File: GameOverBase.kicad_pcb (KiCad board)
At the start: 4 copper layers, 50 x 35 mm, 49 parts, among them J1 USB_C_DEALON-USB-US31-106, J2 Serial Port, J3 add-on conn, Q1 PMN48XP, SW1 SW_DIP_x08, SW2 boot, SW3 Reset, U1 ESP32-WROOM-E, U2 4021, U3 MCP73831-2ACI-OT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

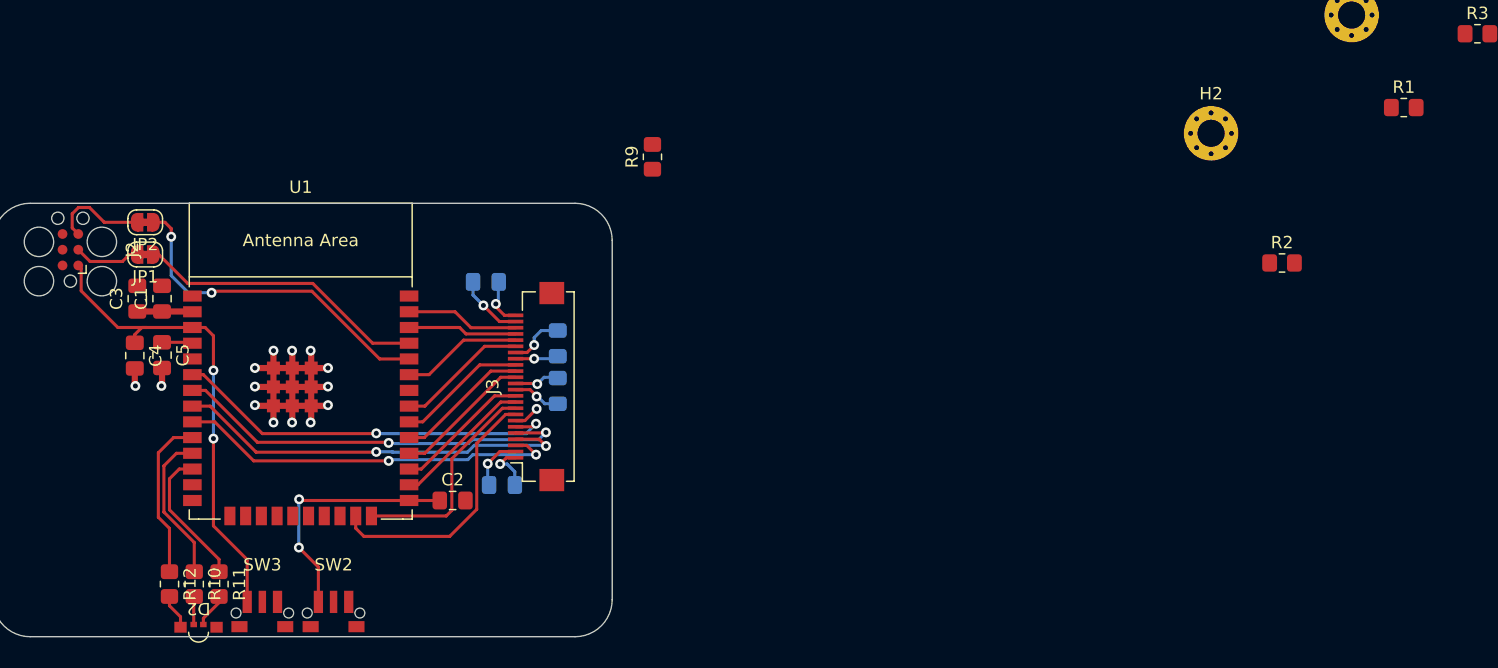
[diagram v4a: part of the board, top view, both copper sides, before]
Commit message: Brings in resistors for the ESP_BOOT and ESP_EN lines that were missing
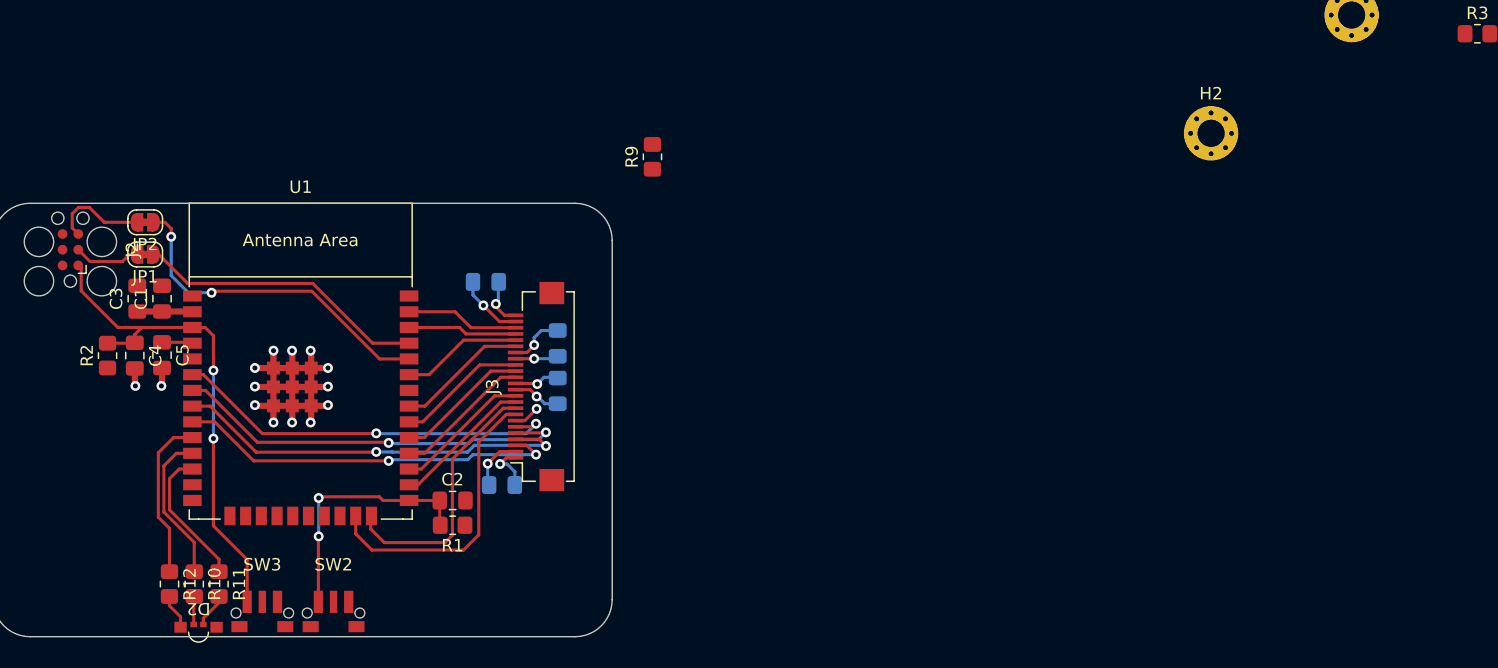
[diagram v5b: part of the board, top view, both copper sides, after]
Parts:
- moved R2 95.1 mm to (129.2, 92.3), turned to 90 degrees
- moved R1 83.9 mm to (157.1, 106.0), turned to 180 degrees
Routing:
- net IO2: track 17.7 -> 21.3 mm
- net IO15: track 21.4 -> 23.8 mm
- net ESP_EN: track 38.8 -> 41.0 mm
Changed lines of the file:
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@@
   )
   (footprint "Resistor_SMD:R_0805_2012Metric_Pad1.20x1.40mm_HandSolder" (layer "F.Cu")
-    (at 233.92 72.27)
+    (at 157.1125 106 180)
     (descr "Resistor SMD 0805 (2012 Metric), square (rectangular) end terminal, IPC_7351 nominal with elongated pad for handsoldering. (Body size source: IPC-SM-782 page 72, https://www.pcb-3d.com/wordpress/wp-content/uploads/ipc-sm-782a_amendment_1_and_2.pdf), generated with kicad-footprint-generator")
     (tags "resistor handsolder")
@@
     (fp_line (start 1 0.625) (end -1 0.625)
       (stroke (width 0.1) (type solid)) (layer "F.Fab"))
-    (pad "1" smd roundrect (at -1 0) (size 1.2 1.4) (layers "F.Cu" "F.Paste" "F.Mask") (roundrect_rratio 0.208333)
+    (pad "1" smd roundrect (at -1 0 180) (size 1.2 1.4) (layers "F.Cu" "F.Paste" "F.Mask") (roundrect_rratio 0.208333)
       (net 3 "+3V3") (pintype "passive"))
-    (pad "2" smd roundrect (at 1 0) (size 1.2 1.4) (layers "F.Cu" "F.Paste" "F.Mask") (roundrect_rratio 0.208333)
+    (pad "2" smd roundrect (at 1 0 180) (size 1.2 1.4) (layers "F.Cu" "F.Paste" "F.Mask") (roundrect_rratio 0.208333)
       (net 4 "ESP_BOOT") (pintype "passive"))
     (model "${KICAD6_3DMODEL_DIR}/Resistor_SMD.3dshapes/R_0805_2012Metric.wrl"
@@
   )
   (footprint "Resistor_SMD:R_0805_2012Metric_Pad1.20x1.40mm_HandSolder" (layer "F.Cu")
-    (at 224.09 84.82)
+    (at 129.25 92.3 90)
     (descr "Resistor SMD 0805 (2012 Metric), square (rectangular) end terminal, IPC_7351 nominal with elongated pad for handsoldering. (Body size source: IPC-SM-782 page 72, https://www.pcb-3d.com/wordpress/wp-content/uploads/ipc-sm-782a_amendment_1_and_2.pdf), generated with kicad-footprint-generator")
     (tags "resistor handsolder")
@@
     (property "Sheetname" "")
     (attr smd)
-    (fp_text reference "R2" (at 0 -1.65) (layer "F.SilkS")
-        (effects (font (size 1 1) (thickness 0.15)))
-    )
-    (fp_text value "10kΩ" (at 0 1.65) (layer "F.Fab")
-        (effects (font (size 1 1) (thickness 0.15)))
-    )
-    (fp_text user "${REFERENCE}" (at 0 0) (layer "F.Fab")
+    (fp_text reference "R2" (at 0 -1.65 90) (layer "F.SilkS")
+        (effects (font (size 1 1) (thickness 0.15)))
+    )
+    (fp_text value "10kΩ" (at 0 1.65 90) (layer "F.Fab")
+        (effects (font (size 1 1) (thickness 0.15)))
+    )
+    (fp_text user "${REFERENCE}" (at 0 0 90) (layer "F.Fab")
         (effects (font (size 0.5 0.5) (thickness 0.08)))
     )
@@
     (fp_line (start 1 0.625) (end -1 0.625)
       (stroke (width 0.1) (type solid)) (layer "F.Fab"))
-    (pad "1" smd roundrect (at -1 0) (size 1.2 1.4) (layers "F.Cu" "F.Paste" "F.Mask") (roundrect_rratio 0.208333)
+    (pad "1" smd roundrect (at -1 0 90) (size 1.2 1.4) (layers "F.Cu" "F.Paste" "F.Mask") (roundrect_rratio 0.208333)
       (net 3 "+3V3") (pintype "passive"))
-    (pad "2" smd roundrect (at 1 0) (size 1.2 1.4) (layers "F.Cu" "F.Paste" "F.Mask") (roundrect_rratio 0.208333)
+    (pad "2" smd roundrect (at 1 0 90) (size 1.2 1.4) (layers "F.Cu" "F.Paste" "F.Mask") (roundrect_rratio 0.208333)
       (net 5 "ESP_EN") (pintype "passive"))
     (model "${KICAD6_3DMODEL_DIR}/Resistor_SMD.3dshapes/R_0805_2012Metric.wrl"
@@
   (segment (start 158.7625 87.4125) (end 158.7625 86.35) (width 0.25) (layer "B.Cu") (net 3))
   (segment (start 161.504472 101.054472) (end 162.1375 101.6875) (width 0.25) (layer "B.Cu") (net 3))
+  (segment (start 151.5 104) (end 153.6 104) (width 0.25) (layer "F.Cu") (net 4))
   (segment (start 153.6 104) (end 156.075 104) (width 0.25) (layer "F.Cu") (net 4))
-  (segment (start 144.7 107.8) (end 146.275 109.375) (width 0.25) (layer "F.Cu") (net 4))
-  (segment (start 144.816179 104) (end 153.6 104) (width 0.25) (layer "F.Cu") (net 4))
-  (segment (start 144.719653 103.903474) (end 144.816179 104) (width 0.25) (layer "F.Cu") (net 4))
-  (segment (start 146.275 109.375) (end 146.275 112.1875) (width 0.25) (layer "F.Cu") (net 4))
-  (via (at 144.7 107.8) (size 0.8) (drill 0.4) (layers "F.Cu" "B.Cu") (net 4))
-  (via (at 144.719653 103.903474) (size 0.8) (drill 0.4) (layers "F.Cu" "B.Cu") (net 4))
-  (segment (start 144.7 107.8) (end 144.7 103.923127) (width 0.25) (layer "B.Cu") (net 4))
-  (segment (start 144.7 103.923127) (end 144.719653 103.903474) (width 0.25) (layer "B.Cu") (net 4))
+  (segment (start 146.4 103.7) (end 151.2 103.7) (width 0.25) (layer "F.Cu") (net 4))
+  (segment (start 156.075 105.9625) (end 156.1125 106) (width 0.25) (layer "F.Cu") (net 4))
+  (segment (start 146.3 106.9) (end 146.275 106.925) (width 0.25) (layer "F.Cu") (net 4))
+  (segment (start 151.2 103.7) (end 151.5 104) (width 0.25) (layer "F.Cu") (net 4))
+  (segment (start 146.3 103.8) (end 146.4 103.7) (width 0.25) (layer "F.Cu") (net 4))
+  (segment (start 146.275 106.925) (end 146.275 112.1875) (width 0.25) (layer "F.Cu") (net 4))
+  (segment (start 156.075 104) (end 156.075 105.9625) (width 0.25) (layer "F.Cu") (net 4))
+  (via (at 146.3 106.9) (size 0.8) (drill 0.4) (layers "F.Cu" "B.Cu") (net 4))
+  (via (at 146.3 103.8) (size 0.8) (drill 0.4) (layers "F.Cu" "B.Cu") (net 4))
+  (segment (start 146.3 103.8) (end 146.3 106.9) (width 0.25) (layer "B.Cu") (net 4))
+  (segment (start 131.4125 91.3) (end 131.45 91.2625) (width 0.25) (layer "F.Cu") (net 5))
   (segment (start 137.8 106.05) (end 140.525 108.775) (width 0.25) (layer "F.Cu") (net 5))
   (segment (start 137.8 90.7) (end 137.13 90.03) (width 0.25) (layer "F.Cu") (net 5))
@@
   (segment (start 140.525 108.775) (end 140.525 112.1875) (width 0.25) (layer "F.Cu") (net 5))
   (segment (start 132.68 90.03) (end 136.1 90.03) (width 0.25) (layer "F.Cu") (net 5))
+  (segment (start 129.25 91.3) (end 131.4125 91.3) (width 0.25) (layer "F.Cu") (net 5))
   (segment (start 126.885 85.02) (end 127.119821 85.254821) (width 0.25) (layer "F.Cu") (net 5))
   (segment (start 137.13 90.03) (end 136.1 90.03) (width 0.25) (layer "F.Cu") (net 5))
@@
   (segment (start 131.64 81.535) (end 128.985 81.535) (width 0.25) (layer "F.Cu") (net 18))
   (segment (start 127.790179 80.340179) (end 126.905707 80.340179) (width 0.25) (layer "F.Cu") (net 18))
-  (segment (start 157.05 104.8) (end 157.05 100.635718) (width 0.25) (layer "F.Cu") (net 19))
-  (segment (start 157.05 100.635718) (end 161.135718 96.55) (width 0.25) (layer "F.Cu") (net 19))
-  (segment (start 156.6 105.25) (end 157.05 104.8) (width 0.25) (layer "F.Cu") (net 19))
-  (segment (start 161.135718 96.55) (end 162.2 96.55) (width 0.25) (layer "F.Cu") (net 19))
-  (segment (start 150.56 105.25) (end 156.6 105.25) (width 0.25) (layer "F.Cu") (net 19))
+  (segment (start 150.5 105.31) (end 150.56 105.25) (width 0.25) (layer "F.Cu") (net 19))
+  (segment (start 150.5 106.3) (end 150.5 105.31) (width 0.25) (layer "F.Cu") (net 19))
+  (segment (start 157.1 106.8) (end 156.5 107.4) (width 0.25) (layer "F.Cu") (net 19))
+  (segment (start 161.2 96.55) (end 157.1 100.65) (width 0.25) (layer "F.Cu") (net 19))
+  (segment (start 156.5 107.4) (end 151.6 107.4) (width 0.25) (layer "F.Cu") (net 19))
+  (segment (start 151.6 107.4) (end 150.5 106.3) (width 0.25) (layer "F.Cu") (net 19))
+  (segment (start 162.2 96.55) (end 161.2 96.55) (width 0.25) (layer "F.Cu") (net 19))
+  (segment (start 157.1 100.65) (end 157.1 106.8) (width 0.25) (layer "F.Cu") (net 19))
   (segment (start 153.6 102.73) (end 154.32 102.73) (width 0.25) (layer "F.Cu") (net 20))
   (segment (start 161 96.05) (end 162.2 96.05) (width 0.25) (layer "F.Cu") (net 20))
@@
   (segment (start 153.6 98.92) (end 154.83 98.92) (width 0.25) (layer "F.Cu") (net 21))
   (segment (start 154.83 98.92) (end 160.2 93.55) (width 0.25) (layer "F.Cu") (net 21))
-  (segment (start 156.874993 106.9) (end 159.06202 104.712973) (width 0.25) (layer "F.Cu") (net 22))
-  (segment (start 149.29 105.25) (end 149.29 106.24) (width 0.25) (layer "F.Cu") (net 22))
-  (segment (start 161.4 97.05) (end 162.2 97.05) (width 0.25) (layer "F.Cu") (net 22))
-  (segment (start 149.29 106.24) (end 149.95 106.9) (width 0.25) (layer "F.Cu") (net 22))
-  (segment (start 149.95 106.9) (end 156.874993 106.9) (width 0.25) (layer "F.Cu") (net 22))
-  (segment (start 159.06202 99.38798) (end 161.4 97.05) (width 0.25) (layer "F.Cu") (net 22))
-  (segment (start 159.06202 104.712973) (end 159.06202 99.38798) (width 0.25) (layer "F.Cu") (net 22))
+  (segment (start 159.225489 99.274511) (end 161.45 97.05) (width 0.25) (layer "F.Cu") (net 22))
+  (segment (start 149.29 105.25) (end 149.29 106.69) (width 0.25) (layer "F.Cu") (net 22))
+  (segment (start 150.6 108) (end 158 108) (width 0.25) (layer "F.Cu") (net 22))
+  (segment (start 149.29 106.69) (end 150.6 108) (width 0.25) (layer "F.Cu") (net 22))
+  (segment (start 158 108) (end 159.225489 106.774511) (width 0.25) (layer "F.Cu") (net 22))
+  (segment (start 159.225489 106.774511) (end 159.225489 99.274511) (width 0.25) (layer "F.Cu") (net 22))
+  (segment (start 161.45 97.05) (end 162.2 97.05) (width 0.25) (layer "F.Cu") (net 22))
   (segment (start 160.5 95.55) (end 154.59 101.46) (width 0.25) (layer "F.Cu") (net 23))
   (segment (start 154.59 101.46) (end 153.6 101.46) (width 0.25) (layer "F.Cu") (net 23))

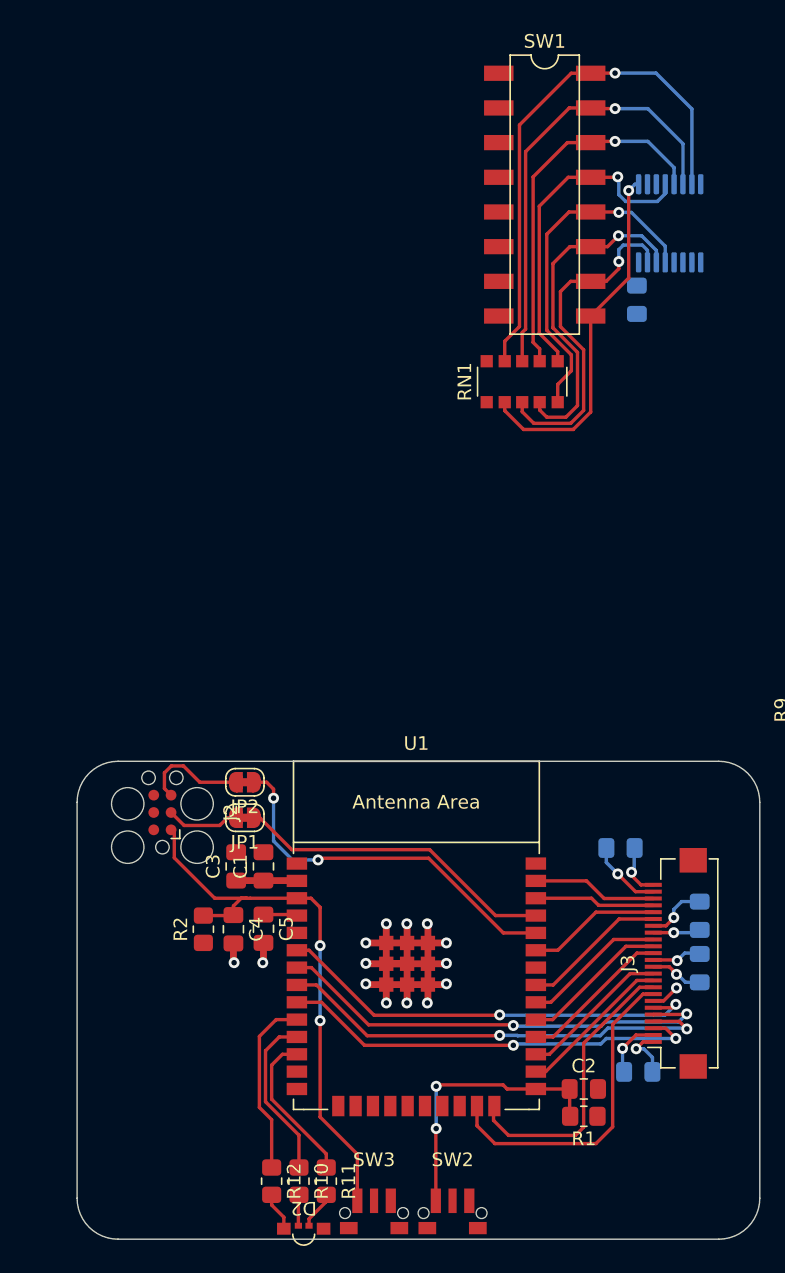
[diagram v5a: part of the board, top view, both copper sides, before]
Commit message: Brings in DIP switches
To route this I needed to swap around the pins on the latch and clock
lines for the 4021 and also the RGB led.
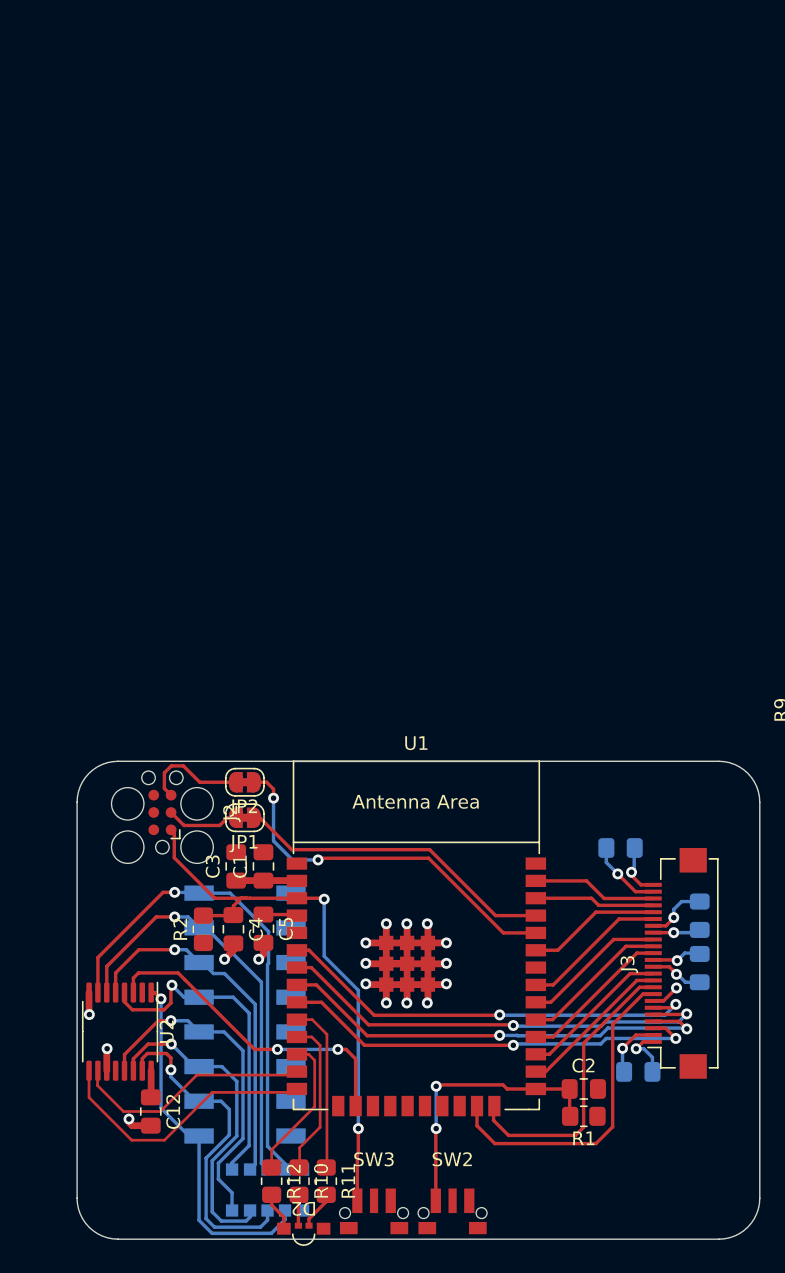
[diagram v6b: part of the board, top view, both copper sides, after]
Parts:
- C12, U2: moved to F.Cu
- RN1, SW1: moved to B.Cu
- moved U2 71.6 mm to (123.1, 99.8)
- moved C12 69.3 mm to (125.4, 105.7)
- moved SW1 63.9 mm to (132.3, 98.5), turned to 180 degrees
- moved RN1 62.1 mm to (133.9, 111.4)
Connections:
- U1 pad 10: BAT_IND_B -> BAT_IND_G
- U1 pad 12: BAT_IND_G -> BAT_IND_B
- U1 pad 13: ID_LATCH -> ID_CLK
- U1 pad 14: ID_CLK -> ID_LATCH
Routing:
- net ID_DATA: track 0.00 -> 23.6 mm, vias 0 -> 2
- net ID_LATCH: track 0.00 -> 19.9 mm
- net ID_CLK: track 0.00 -> 17.6 mm
- net GND: track 58.3 -> 63.2 mm, vias 19 -> 22
- net BAT_IND_B: track 13.2 -> 10.6 mm
- net Net-(RN1-R8): track 38.5 -> 36.2 mm
- net +3V3: track 21.2 -> 23.2 mm
- net Net-(RN1-R7): track 32.4 -> 30.8 mm
- net BAT_IND_G: track 11.3 -> 12.4 mm
- net Net-(RN1-R6): track 27.1 -> 26.3 mm
- net Net-(RN1-R3): track 24.8 -> 24.0 mm
- net BAT_IND_R: track 12.3 -> 11.5 mm
- net Net-(RN1-R2): track 25.0 -> 24.3 mm
- net ESP_EN: track 41.0 -> 41.6 mm
